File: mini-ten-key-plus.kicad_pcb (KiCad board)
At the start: 2 copper layers, 95.2 x 95.2 mm, 64 parts, among them SW0 SW_Push, U0 ProMicro

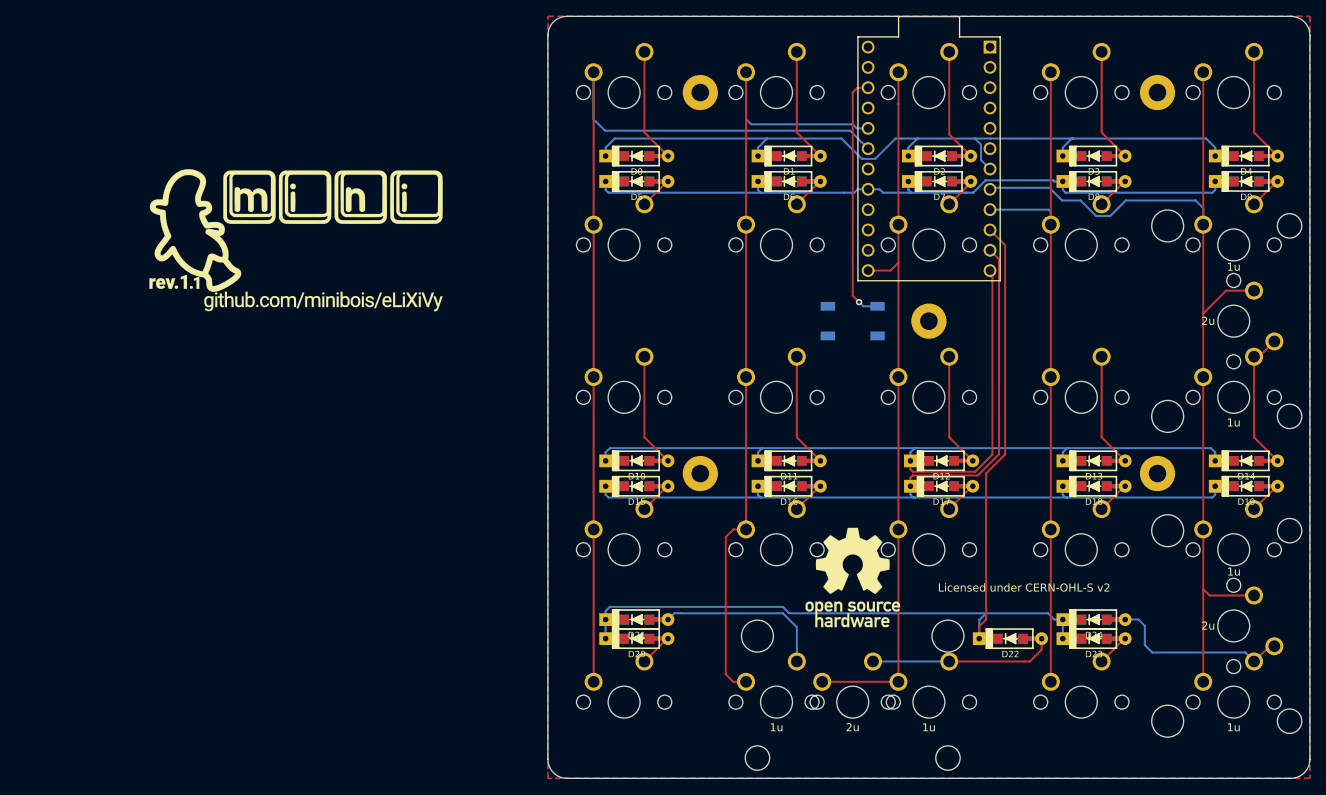
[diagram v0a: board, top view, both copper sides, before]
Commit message: Added rotary encoder
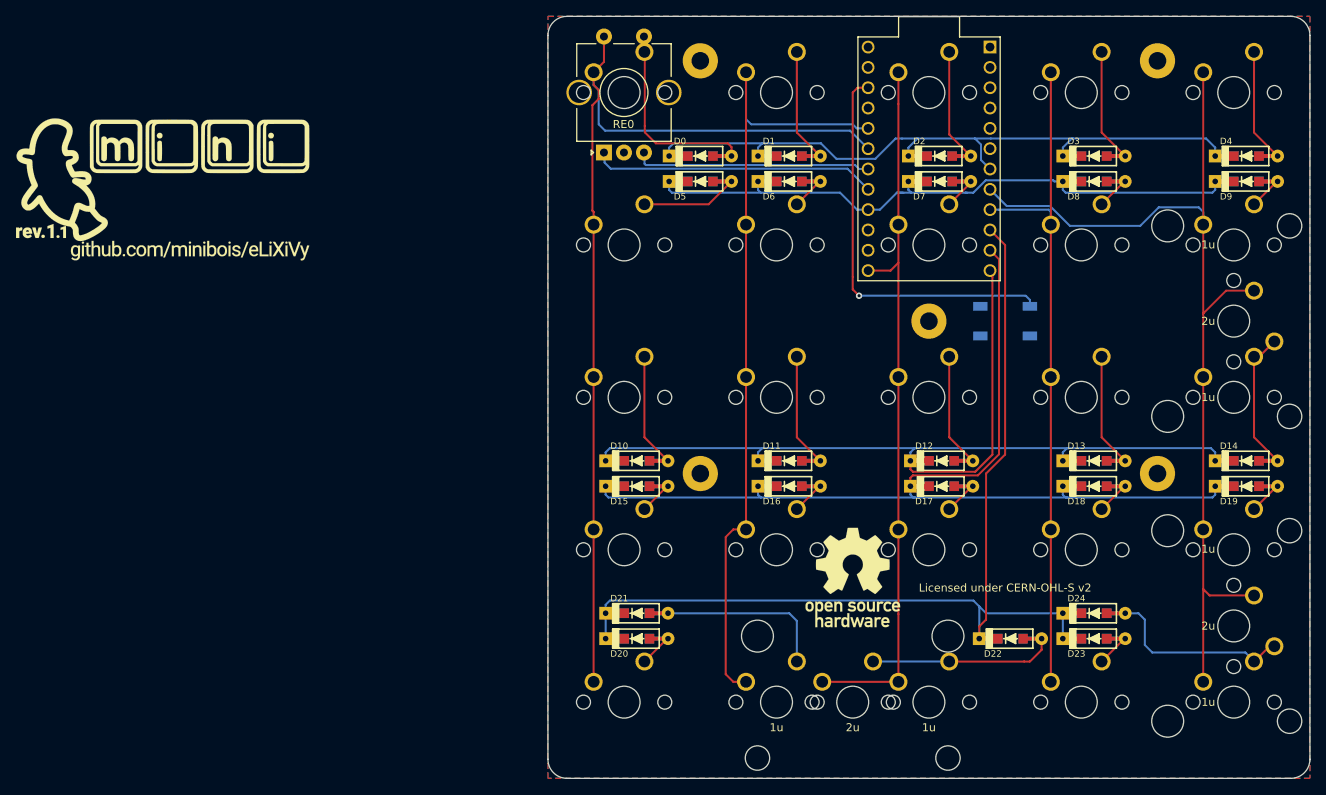
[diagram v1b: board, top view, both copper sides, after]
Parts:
- added RE0: Rotary_Encoder_Switch, mini-general-tweaks:RotaryEncoder_Alps_EC11E-Switch-Vertical-EDIT, F.Cu at (195.1, 86.1)
- moved SW0 19.1 mm to (245.3, 107.2)
- moved LO0 17.8 mm to (140.0, 90.8)
- moved LO1 17.8 mm to (140.0, 90.8)
- moved D0 7.94 mm to (207.2, 86.5)
- moved D5 7.94 mm to (207.2, 89.7)
- moved H0 3.97 mm to (264.3, 74.6)
- moved H4 3.97 mm to (207.2, 74.6)
- moved D21 0.79 mm to (199.2, 143.7)
- moved D24 0.79 mm to (256.4, 143.7)
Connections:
- net Net-(D0-Pad2) renamed ROW0_RE
- U0 pad 16: Net-(U0-Pad16) -> ROW1
- U0 pad 17: ROW1 -> RE+
- U0 pad 18: Net-(U0-Pad18) -> RE-
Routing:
- net RE+: track 0.00 -> 35.6 mm
- net RE-: track 0.00 -> 29.6 mm
- net RESET: track 31.2 -> 50.3 mm
- net ROW0_RE: track 14.2 -> 24.7 mm
- net ROW0: track 94.3 -> 85.0 mm
- net Net-(D5-Pad2): track 4.13 -> 12.1 mm
- net ROW1: track 84.1 -> 78.4 mm
- net COL0: track 117.9 -> 123.6 mm
- net ROW4: track 120.6 -> 122.7 mm
- net Net-(D24-Pad2): track 23.0 -> 23.8 mm

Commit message: Added TKP logo, restructured schematic
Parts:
- LO0: footprint mini-Logos:eLiXiVy-rev1.1-SilkScreen -> mini-Logos:mini-TKP-BSilk
- LO1: footprint mini-Logos:eLiXiVy-rev1.1-Mask -> mini-Logos:mini-TKP-BMask
- LO2: moved to B.Cu
- moved LO0 74.4 mm to (213.0, 105.2)
- moved LO1 74.4 mm to (213.0, 105.2)
- turned LO2 to 180 degrees
- renumbered SW0 to RESET
